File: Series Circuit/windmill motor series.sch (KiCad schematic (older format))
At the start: 9 parts

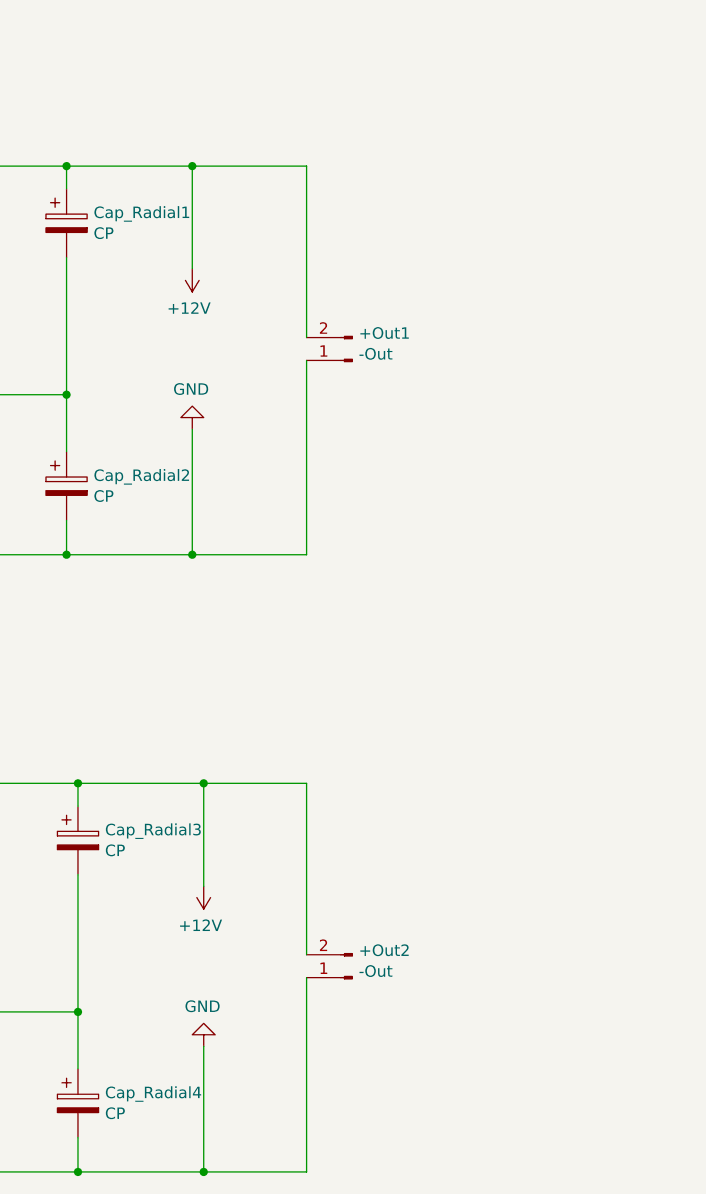
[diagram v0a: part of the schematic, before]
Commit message: Separate out power flags and add jumpers to allow tied operation.
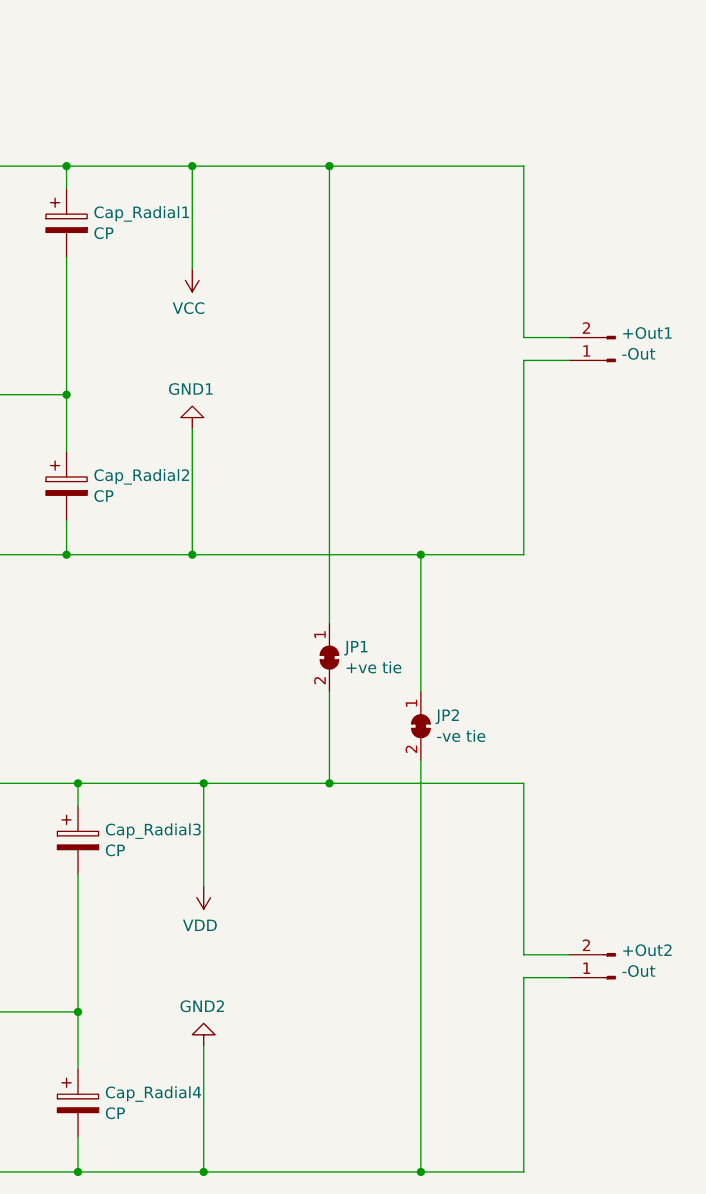
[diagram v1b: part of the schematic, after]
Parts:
- added JP1: +ve tie, Jumper:SolderJumper-2_P1.3mm_Bridged_RoundedPad1.0x1.5mm, symbol Jumper:SolderJumper_2_Bridged
- added JP2: -ve tie, Jumper:SolderJumper-2_P1.3mm_Bridged_RoundedPad1.0x1.5mm, symbol Jumper:SolderJumper_2_Bridged
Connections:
- net +12V renamed VCC
- net VCC: now also JP1.1 (A); no longer +Out2.2 (Pin_2), BridgeRectifier2.1 (+), Cap_Radial3.1
- net GND renamed GND1
- net GND1: now also JP2.1 (A); no longer +Out2.1 (Pin_1), BridgeRectifier2.4 (-), Cap_Radial4.2
- new net GND2: +Out2.1 (Pin_1), BridgeRectifier2.4 (-), Cap_Radial4.2, JP2.2 (B)
- new net VDD: +Out2.2 (Pin_2), BridgeRectifier2.1 (+), Cap_Radial3.1, JP1.2 (B)
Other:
- moved on the sheet: +Out1, +Out2
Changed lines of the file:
@@
 EESchema Schematic File Version 4
-LIBS:windmill motor series-cache
-EELAYER 29 0
+EELAYER 30 0
 EELAYER END
 $Descr A4 11693 8268
@@
 Connection ~ 6850 3450
 $Comp
-L power:GND #PWR0101
-U 1 1 61012945
-P 7400 2900
-F 0 "#PWR0101" H 7400 2650 50  0001 C CNN
-F 1 "GND" H 7405 2727 50  0000 C CNN
-F 2 "" H 7400 2900 50  0001 C CNN
-F 3 "" H 7400 2900 50  0001 C CNN
-	1    7400 2900
-	-1   0    0    1
-$EndComp
-$Comp
-L power:+12V #PWR0102
-U 1 1 61013073
-P 7400 2200
-F 0 "#PWR0102" H 7400 2050 50  0001 C CNN
-F 1 "+12V" H 7415 2373 50  0000 C CNN
-F 2 "" H 7400 2200 50  0001 C CNN
-F 3 "" H 7400 2200 50  0001 C CNN
-	1    7400 2200
-	-1   0    0    1
-$EndComp
-$Comp
 L Device:D_Bridge_+AA- BridgeRectifier2
 U 1 1 61015125
@@
 	7450 6150 7450 5600
 Connection ~ 6900 6150
-$Comp
-L power:GND #PWR0103
-U 1 1 61015159
-P 7450 5600
-F 0 "#PWR0103" H 7450 5350 50  0001 C CNN
-F 1 "GND" H 7455 5427 50  0000 C CNN
-F 2 "" H 7450 5600 50  0001 C CNN
-F 3 "" H 7450 5600 50  0001 C CNN
-	1    7450 5600
-	-1   0    0    1
-$EndComp
-$Comp
-L power:+12V #PWR0104
-U 1 1 61015163
-P 7450 4900
-F 0 "#PWR0104" H 7450 4750 50  0001 C CNN
-F 1 "+12V" H 7465 5073 50  0000 C CNN
-F 2 "" H 7450 4900 50  0001 C CNN
-F 3 "" H 7450 4900 50  0001 C CNN
-	1    7450 4900
-	-1   0    0    1
-$EndComp
 Wire Wire Line
 	4500 3700 2100 3700
@@
 L Connector:Conn_01x02_Male +Out1
 U 1 1 6101AECC
-P 8100 2600
-F 0 "+Out1" H 8072 2482 50  0000 R CNN
-F 1 "-Out" H 8072 2573 50  0000 R CNN
-F 2 "Connectors_WAGO:WAGO_734_2pin_Straight_RuggedPads" H 8100 2600 50  0001 C CNN
-F 3 "~" H 8100 2600 50  0001 C CNN
-	1    8100 2600
+P 9250 2600
+F 0 "+Out1" H 9222 2482 50  0000 R CNN
+F 1 "-Out" H 9222 2573 50  0000 R CNN
+F 2 "Connectors_WAGO:WAGO_734_2pin_Straight_RuggedPads" H 9250 2600 50  0001 C CNN
+F 3 "~" H 9250 2600 50  0001 C CNN
+	1    9250 2600
 	-1   0    0    1
 $EndComp
@@
 L Connector:Conn_01x02_Male +Out2
 U 1 1 6101CD8E
-P 8100 5300
-F 0 "+Out2" H 8072 5182 50  0000 R CNN
-F 1 "-Out" H 8072 5273 50  0000 R CNN
-F 2 "Connectors_WAGO:WAGO_734_2pin_Straight_RuggedPads" H 8100 5300 50  0001 C CNN
-F 3 "~" H 8100 5300 50  0001 C CNN
-	1    8100 5300
-	-1   0    0    1
-$EndComp
-Wire Wire Line
-	7400 1750 7900 1750
-Wire Wire Line
-	7900 1750 7900 2500
+P 9250 5300
+F 0 "+Out2" H 9222 5182 50  0000 R CNN
+F 1 "-Out" H 9222 5273 50  0000 R CNN
+F 2 "Connectors_WAGO:WAGO_734_2pin_Straight_RuggedPads" H 9250 5300 50  0001 C CNN
+F 3 "~" H 9250 5300 50  0001 C CNN
+	1    9250 5300
+	-1   0    0    1
+$EndComp
 Connection ~ 7400 1750
-Wire Wire Line
-	7900 2600 7900 3450
 Wire Wire Line
 	6850 3450 7400 3450
 Connection ~ 7400 3450
-Wire Wire Line
-	7400 3450 7900 3450
-Wire Wire Line
-	7450 4450 7900 4450
-Wire Wire Line
-	7900 4450 7900 5200
 Connection ~ 7450 4450
-Wire Wire Line
-	7900 5300 7900 6150
-Wire Wire Line
-	7900 6150 7450 6150
 Connection ~ 7450 6150
 $Comp
@@
 	1    0    0    -1
 $EndComp
+$Comp
+L power:GND1 #PWR02
+U 1 1 6101AC1F
+P 7400 2900
+F 0 "#PWR02" H 7400 2650 50  0001 C CNN
+F 1 "GND1" H 7405 2727 50  0000 C CNN
+F 2 "" H 7400 2900 50  0001 C CNN
+F 3 "" H 7400 2900 50  0001 C CNN
+	1    7400 2900
+	-1   0    0    1
+$EndComp
+$Comp
+L power:GND2 #PWR04
+U 1 1 6101D1AC
+P 7450 5600
+F 0 "#PWR04" H 7450 5350 50  0001 C CNN
+F 1 "GND2" H 7455 5427 50  0000 C CNN
+F 2 "" H 7450 5600 50  0001 C CNN
+F 3 "" H 7450 5600 50  0001 C CNN
+	1    7450 5600
+	-1   0    0    1
+$EndComp
+$Comp
+L power:VCC #PWR01
+U 1 1 6101DA99
+P 7400 2200
+F 0 "#PWR01" H 7400 2050 50  0001 C CNN
+F 1 "VCC" H 7415 2373 50  0000 C CNN
+F 2 "" H 7400 2200 50  0001 C CNN
+F 3 "" H 7400 2200 50  0001 C CNN
+	1    7400 2200
+	-1   0    0    1
+$EndComp
+$Comp
+L power:VDD #PWR03
+U 1 1 6101ED7E
+P 7450 4900
+F 0 "#PWR03" H 7450 4750 50  0001 C CNN
+F 1 "VDD" H 7465 5073 50  0000 C CNN
+F 2 "" H 7450 4900 50  0001 C CNN
+F 3 "" H 7450 4900 50  0001 C CNN
+	1    7450 4900
+	-1   0    0    1
+$EndComp
+$Comp
+L Jumper:SolderJumper_2_Bridged JP1
+U 1 1 61027298
+P 8000 3900
+F 0 "JP1" V 7954 3968 50  0000 L CNN
+F 1 "+ve tie" V 8045 3968 50  0000 L CNN
+F 2 "Jumper:SolderJumper-2_P1.3mm_Bridged_RoundedPad1.0x1.5mm" H 8000 3900 50  0001 C CNN
+F 3 "~" H 8000 3900 50  0001 C CNN
+	1    8000 3900
+	0    1    1    0
+$EndComp
+$Comp
+L Jumper:SolderJumper_2_Bridged JP2
+U 1 1 6102784D
+P 8400 4200
+F 0 "JP2" V 8354 4268 50  0000 L CNN
+F 1 "-ve tie" V 8445 4268 50  0000 L CNN
+F 2 "Jumper:SolderJumper-2_P1.3mm_Bridged_RoundedPad1.0x1.5mm" H 8400 4200 50  0001 C CNN
+F 3 "~" H 8400 4200 50  0001 C CNN
+	1    8400 4200
+	0    1    1    0
+$EndComp
+Wire Wire Line
+	8000 4450 8000 4050
+Wire Wire Line
+	7450 4450 8000 4450
+Wire Wire Line
+	8000 4450 8850 4450
+Wire Wire Line
+	8850 4450 8850 5200
+Wire Wire Line
+	8850 5200 9050 5200
+Connection ~ 8000 4450
+Wire Wire Line
+	8400 3450 8400 4050
+Wire Wire Line
+	7400 3450 8400 3450
+Wire Wire Line
+	8400 4350 8400 6150
+Wire Wire Line
+	7450 6150 8400 6150
+Wire Wire Line
+	8400 6150 8850 6150
+Wire Wire Line
+	8850 6150 8850 5300
+Wire Wire Line
+	8850 5300 9050 5300
+Connection ~ 8400 6150
+Wire Wire Line
+	9050 2600 8850 2600
+Wire Wire Line
+	8850 2600 8850 3450
+Wire Wire Line
+	8850 3450 8400 3450
+Connection ~ 8400 3450
+Wire Wire Line
+	9050 2500 8850 2500
+Wire Wire Line
+	8850 2500 8850 1750
+Wire Wire Line
+	7400 1750 8000 1750
+Wire Wire Line
+	8000 3750 8000 1750
+Connection ~ 8000 1750
+Wire Wire Line
+	8000 1750 8850 1750
 $EndSCHEMATC
